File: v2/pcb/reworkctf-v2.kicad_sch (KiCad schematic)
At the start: 35 parts, among them J2 CORTEX_DEBUG_ETM, J6 CONN_01X03, J7 PMOD_HOST, J8 PMOD_HOST, M1 SCREWHOLE, M2 SCREWHOLE, M3 SCREWHOLE, M4 SCREWHOLE, U1 STM32H750XBH6, U3 ECS-1612MV-250-CN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

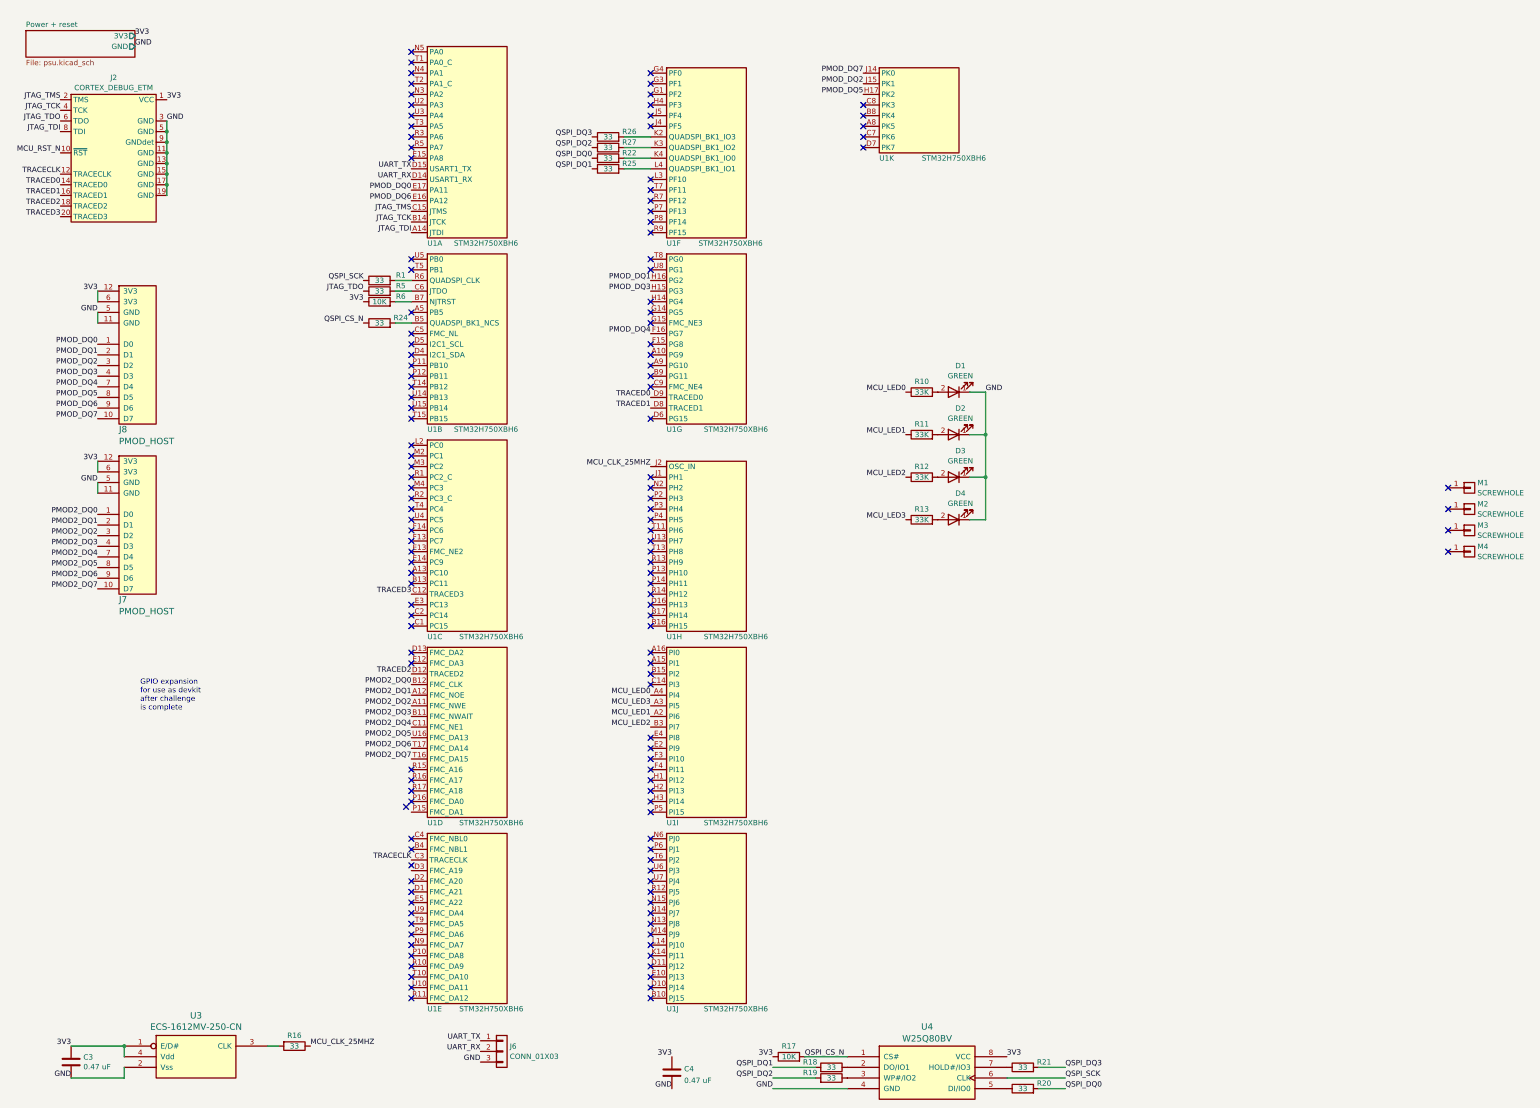
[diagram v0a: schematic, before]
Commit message: Finished initial MCU layout, need to actually add challenges
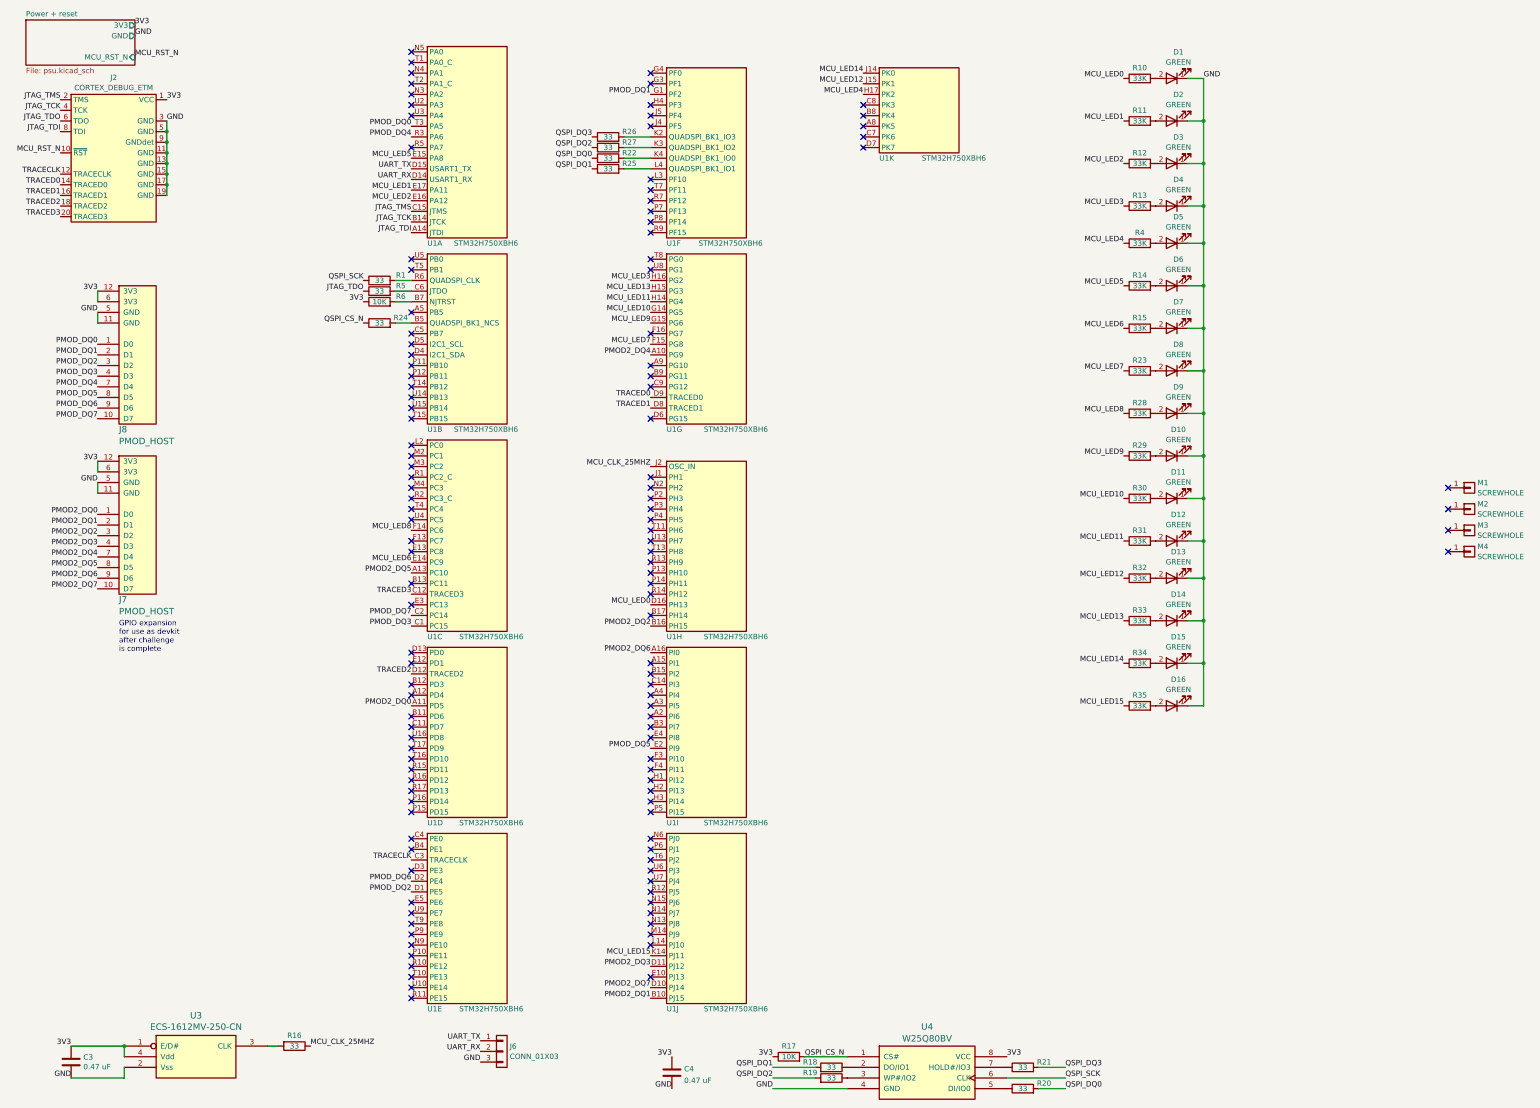
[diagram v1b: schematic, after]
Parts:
- added D10, D11, D12, D13, D14, D15, D16, D5, D6, D7, D8, D9: GREEN, azonenberg_pcb:EIA_0402_LED, symbol device:LED
- added R14, R15, R23, R28, R29, R30, R31, R32, R33, R34, R35, R4: 33K, azonenberg_pcb:EIA_0402_RES_NOSILK, symbol device:R
- M1, M2, M3, M4: footprint (none) -> azonenberg_pcb:MECHANICAL_CLEARANCEHOLE_4_40
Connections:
- net GND: now also D10.1 (K), D11.1 (K), D12.1 (K), D13.1 (K), D14.1 (K), D15.1 (K), D16.1 (K), D5.1 (K), D6.1 (K), D7.1 (K), D8.1 (K), D9.1 (K)
- net MCU_LED0: now also U1.D16 (PH13); no longer U1.A4 (PI4)
- net MCU_LED1: now also U1.E17 (PA11); no longer U1.A2 (PI6)
- net MCU_LED2: now also U1.E16 (PA12); no longer U1.B3 (PI7)
- net MCU_LED3: now also U1.H16 (PG2); no longer U1.A3 (PI5)
- net PMOD2_DQ0: now also U1.A11 (PD5); no longer U1.B12 (PD3)
- net PMOD2_DQ1: now also U1.B10 (PJ15); no longer U1.A12 (PD4)
- net PMOD2_DQ2: now also U1.B16 (PH15); no longer U1.A11 (PD5)
- net PMOD2_DQ3: now also U1.D11 (PJ12); no longer U1.B11 (PD6)
- net PMOD2_DQ4: now also U1.A10 (PG9); no longer U1.C11 (PD7)
- net PMOD2_DQ5: now also U1.A13 (PC10); no longer U1.U16 (PD8)
- net PMOD2_DQ6: now also U1.A16 (PI0); no longer U1.T17 (PD9)
- net PMOD2_DQ7: now also U1.D10 (PJ14); no longer U1.T16 (PD10)
- net PMOD_DQ0: now also U1.T3 (PA5); no longer U1.E17 (PA11)
- net PMOD_DQ1: now also U1.G1 (PF2); no longer U1.H16 (PG2)
- net PMOD_DQ2: now also U1.D1 (PE5); no longer U1.J15 (PK1)
- net PMOD_DQ3: now also U1.C1 (PC15); no longer U1.H15 (PG3)
- net PMOD_DQ4: now also U1.R3 (PA6); no longer U1.F16 (PG7)
- net PMOD_DQ5: now also U1.E2 (PI9); no longer U1.H17 (PK2)
- net PMOD_DQ6: now also U1.D2 (PE4); no longer U1.E16 (PA12)
- net PMOD_DQ7: now also U1.C2 (PC14); no longer U1.J14 (PK0)
- net MCU_LED5: now reaches U1.E15 (PA8)
- net MCU_LED5: now also R14.1
- net MCU_LED7: now reaches U1.F15 (PG8)
- net MCU_LED7: now also R23.1
- net MCU_LED10: now reaches U1.G14 (PG5)
- net MCU_LED10: now also R30.1
- net MCU_LED9: now reaches U1.G15 (PG6)
- net MCU_LED9: now also R29.1
- net MCU_LED11: now reaches U1.H14 (PG4)
- net MCU_LED11: now also R31.1
- net MCU_LED15: now reaches U1.K14 (PJ11)
- net MCU_LED15: now also R35.1
- net MCU_LED6: now reaches U1.E14 (PC9)
- net MCU_LED6: now also R15.1
- net MCU_LED8: now reaches U1.F14 (PC6)
- net MCU_LED8: now also R28.1
- new net: D13.2 (A), R32.2
- new net: D15.2 (A), R34.2
- new net: D9.2 (A), R28.2
- new net: D7.2 (A), R15.2
- new net: D10.2 (A), R29.2
- new net: D6.2 (A), R14.2
- new net: D11.2 (A), R30.2
- new net: D12.2 (A), R31.2
- new net: D14.2 (A), R33.2
- new net: D5.2 (A), R4.2
- new net: D16.2 (A), R35.2
- new net: D8.2 (A), R23.2
- new net MCU_LED12: R32.1, U1.J15 (PK1)
- new net MCU_LED13: R33.1, U1.H15 (PG3)
- new net MCU_LED14: R34.1, U1.J14 (PK0)
- new net MCU_LED4: R4.1, U1.H17 (PK2)
- no-connect marks 137 -> 125
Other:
- sheet Power + reset ports: added MCU_RST_N; removed none
- moved on the sheet: D1, D2, D3, D4, R10, R11, R12, R13

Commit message: Got up to challenge 8
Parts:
- added J3: DOT, azonenberg_pcb:TESTPOINT_SMT_0.5MM, symbol conn:CONN_01X01
- added R36: 10K, azonenberg_pcb:EIA_0201_RES_NOSILK, symbol device:R
- added R37: 10K, azonenberg_pcb:EIA_01005_RES_NOSILK, symbol device:R
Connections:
- net 3V3: now also R36.1, R37.1
- net GND: now also D3.2 (A); no longer D3.1 (K)
- net CHALLENGE_08_A: now reaches U1.T7 (PF11)
- net CHALLENGE_08_A: now also U1.U8 (PG1)
- net CHALLENGE_02_B: now reaches U1.T5 (PB1)
- net CHALLENGE_02_B: now also U1.U4 (PC5)
- net CHALLENGE_02_A: now reaches U1.U5 (PB0)
- net CHALLENGE_02_A: now also U1.U3 (PA4)
- net CHALLENGE_01: now reaches U1.U2 (PA3)
- net CHALLENGE_01: now also J3.1 (P1)
- net at R12.2: now also D3.1 (K); no longer D3.2 (A)
- net CHALLENGE_04: now reaches U1.U6 (PJ3)
- net CHALLENGE_04: now also R36.2
- net CHALLENGE_05: now reaches U1.U7 (PJ4)
- net CHALLENGE_05: now also R37.2
- no-connect marks 125 -> 116
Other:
- moved on the sheet: D3

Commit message: Added challenge 9 with diffpair polarity swap on inner layer
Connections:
- net CHALLENGE_09_N: now reaches U1.P8 (PF14)
- net CHALLENGE_09_N: now also U1.U9 (PE7)
- net CHALLENGE_09_P: now reaches U1.P9 (PE9)
- net CHALLENGE_09_P: now also U1.U10 (PE14)
- no-connect marks 116 -> 112
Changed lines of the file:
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@@
-	)
-	(no_connect
-		(at 109.22 233.68)
 	)
 	(no_connect
@@
 	)
 	(no_connect
-		(at 109.22 246.38)
-	)
-	(no_connect
 		(at 166.37 100.33)
 	)
@@
 	)
 	(no_connect
-		(at 166.37 63.5)
-	)
-	(no_connect
 		(at 109.22 45.72)
 	)
@@
 	)
 	(no_connect
-		(at 109.22 228.6)
-	)
-	(no_connect
 		(at 166.37 110.49)
 	)
@@
 			(width 0)
 			(type default)
+		)
+	)
+	(label "CHALLENGE_09_P"
+		(at 109.22 233.68 180)
+		(effects
+			(font
+				(size 1.27 1.27)
+			)
+			(justify right bottom)
 		)
 	)
@@
 		)
 	)
+	(label "CHALLENGE_09_N"
+		(at 109.22 228.6 180)
+		(effects
+			(font
+				(size 1.27 1.27)
+			)
+			(justify right bottom)
+		)
+	)
 	(label "UART_TX"
 		(at 109.22 50.8 180)
@@
 		)
 	)
+	(label "CHALLENGE_09_P"
+		(at 109.22 246.38 180)
+		(effects
+			(font
+				(size 1.27 1.27)
+			)
+			(justify right bottom)
+		)
+	)
 	(label "MCU_RST_N"
 		(at 43.18 24.13 0)
@@
 		(effects
 			(font
+				(size 1.27 1.27)
+			)
+			(justify right bottom)
+		)
+	)
+	(label "CHALLENGE_09_N"
+		(at 166.37 63.5 180)
+		(effects
+			(font

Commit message: Added challenges 10 and 11 for vias
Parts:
- added R38: 0, azonenberg_pcb:EIA_0402_RES_NOSILK, symbol device:R
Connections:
- net 3V3: now also R38.2
- net CHALLENGE_10: now reaches U1.R9 (PF15)
- net CHALLENGE_10: now also U1.R10 (PE12)
- net CHALLENGE_11: now reaches U1.T13 (PH8)
- net CHALLENGE_11: now also U1.U13 (PH7), R38.1
- no-connect marks 112 -> 108
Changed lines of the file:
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@@
 	)
 	(no_connect
-		(at 109.22 105.41)
-	)
-	(no_connect
 		(at 109.22 238.76)
 	)
@@
 	)
 	(no_connect
-		(at 166.37 142.24)
-	)
-	(no_connect
 		(at 217.17 45.72)
 	)
@@
 	)
 	(no_connect
-		(at 166.37 66.04)
-	)
-	(no_connect
 		(at 109.22 168.91)
 	)
@@
 	)
 	(no_connect
+		(at 109.22 105.41)
+	)
+	(no_connect
 		(at 217.17 43.18)
 	)
@@
 	)
 	(no_connect
-		(at 109.22 241.3)
-	)
-	(no_connect
 		(at 166.37 100.33)
 	)
@@
 	)
 	(no_connect
-		(at 166.37 139.7)
-	)
-	(no_connect
 		(at 109.22 231.14)
 	)
@@
 		)
 	)
+	(label "CHALLENGE_10"
+		(at 166.37 66.04 180)
+		(effects
+			(font
+				(size 1.27 1.27)
+			)
+			(justify right bottom)
+		)
+	)
 	(label "MCU_LED4"
 		(at 217.17 33.02 180)
@@
 		)
 	)
+	(label "CHALLENGE_11"
+		(at 209.55 133.35 180)
+		(effects
+			(font
+				(size 1.27 1.27)
+			)
+			(justify right bottom)
+		)
+	)
 	(label "MCU_LED12"
 		(at 279.4 148.59 180)
@@
 	)
 	(label "3V3"
+		(at 217.17 133.35 0)
+		(effects
+			(font
+				(size 1.27 1.27)
+			)
+			(justify left bottom)
+		)
+	)
+	(label "3V3"
 		(at 195.58 262.89 180)
 		(effects
@@
 		)
 	)
+	(label "CHALLENGE_11"
+		(at 166.37 139.7 180)
+		(effects
+			(font
+				(size 1.27 1.27)
+			)
+			(justify right bottom)
+		)
+	)
 	(label "CHALLENGE_04"
 		(at 166.37 218.44 180)
@@
 		)
 	)
+	(label "CHALLENGE_11"
+		(at 166.37 142.24 180)
+		(effects
+			(font
+				(size 1.27 1.27)
+			)
+			(justify right bottom)
+		)
+	)
 	(label "MCU_LED5"
 		(at 109.22 48.26 180)
@@
 		)
 	)
+	(label "CHALLENGE_10"
+		(at 109.22 241.3 180)
+		(effects
+			(font
+				(size 1.27 1.27)
+			)
+			(justify right bottom)
+		)
+	)
 	(label "MCU_LED3"
 		(at 166.37 77.47 180)
@@
 				)
 			)
+		)
+	)
+	(symbol
+		(lib_id "device:R")
+		(at 213.36 133.35 90)
+		(unit 1)
+		(exclude_from_sim no)
+		(in_bom yes)
+		(on_board yes)
+		(dnp no)
+		(fields_autoplaced yes)
+		(property "Reference" "R38"
+			(at 213.36 128.1895 90)
+			(effects
+				(font
+					(size 1.27 1.27)
+				)
+			)
+		)
+		(property "Value" "0"
+			(at 213.36 130.6138 90)
+			(effects
+				(font
+					(size 1.27 1.27)
+				)
+			)
+		)
+		(property "Footprint" "azonenberg_pcb:EIA_0402_RES_NOSILK"
+			(at 213.36 135.128 90)
+			(effects
+				(font
+					(size 1.27 1.27)
+				)
+				(hide yes)
+			)
+		)
+		(property "Datasheet" ""
+			(at 213.36 133.35 0)
+			(effects
+				(font
+					(size 1.27 1.27)
+				)
+				(hide yes)
+			)
+		)
+		(property "Description" "Resistor"
+			(at 213.36 133.35 0)
+			(effects
+				(font
+					(size 1.27 1.27)
+				)
+				(hide yes)
+			)
+		)
+		(pin "2"
+		)
+		(pin "1"
+		)
+		(instances
+			(project "reworkctf-v2"
+				(path "/2cafc55c-39dd-4b2d-b0b4-dd03e5652b07"
+					(reference "R38")
+					(unit 1)
+				)
+			)

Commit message: Added SM-2 challenge, shrunk overall PCB footprint a bunch
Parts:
- added M5: OSHW, w_logo:Logo_silk_OSHW_6x6mm, symbol special-azonenberg:MECHANICAL
- added M6: LONGTHING, azonenberg_pcb:LONGTHING-1200DPI, symbol special-azonenberg:MECHANICAL
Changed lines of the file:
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@@
 	)
 	(symbol
+		(lib_id "special-azonenberg:MECHANICAL")
+		(at 360.68 156.21 0)
+		(unit 1)
+		(exclude_from_sim no)
+		(in_bom yes)
+		(on_board yes)
+		(dnp no)
+		(fields_autoplaced yes)
+		(property "Reference" "M6"
+			(at 363.855 154.9978 0)
+			(effects
+				(font
+					(size 1.27 1.27)
+				)
+				(justify left)
+			)
+		)
+		(property "Value" "LONGTHING"
+			(at 363.855 157.4221 0)
+			(effects
+				(font
+					(size 1.27 1.27)
+				)
+				(justify left)
+			)
+		)
+		(property "Footprint" "azonenberg_pcb:LONGTHING-1200DPI"
+			(at 360.68 156.21 0)
+			(effects
+				(font
+					(size 1.27 1.27)
+				)
+				(hide yes)
+			)
+		)
+		(property "Datasheet" ""
+			(at 360.68 156.21 0)
+			(effects
+				(font
+					(size 1.27 1.27)
+				)
+				(hide yes)
+			)
+		)
+		(property "Description" ""
+			(at 360.68 156.21 0)
+			(effects
+				(font
+					(size 1.27 1.27)
+				)
+				(hide yes)
+			)
+		)
+		(instances
+			(project "reworkctf-v2"
+				(path "/2cafc55c-39dd-4b2d-b0b4-dd03e5652b07"
+					(reference "M6")
+					(unit 1)
+				)
+			)
+		)
+	)
+	(symbol
 		(lib_id "device:R")
 		(at 283.21 119.38 90)
@@
 					(unit 1)
 				)
+			)
+		)
+	)
+	(symbol
+		(lib_id "special-azonenberg:MECHANICAL")
+		(at 360.68 149.86 0)
+		(unit 1)
+		(exclude_from_sim no)
+		(in_bom yes)
+		(on_board yes)
+		(dnp no)
+		(fields_autoplaced yes)
+		(property "Reference" "M5"
+			(at 363.855 148.6478 0)
+			(effects
+				(font
+					(size 1.27 1.27)
+				)
+				(justify left)
+			)
+		)
+		(property "Value" "OSHW"
+			(at 363.855 151.0721 0)
+			(effects
+				(font
+					(size 1.27 1.27)
+				)
+				(justify left)
+			)
+		)
+		(property "Footprint" "w_logo:Logo_silk_OSHW_6x6mm"
+			(at 360.68 149.86 0)
+			(effects
+				(font
+					(size 1.27 1.27)
+				)
+				(hide yes)
+			)
+		)
+		(property "Datasheet" ""
+			(at 360.68 149.86 0)
+			(effects
+				(font
+					(size 1.27 1.27)
+				)
+				(hide yes)
+			)
+		)
+		(property "Description" ""
+			(at 360.68 149.86 0)
+			(effects
+				(font
+					(size 1.27 1.27)
+				)
+				(hide yes)
+			)
+		)
+		(instances
+			(project "reworkctf-v2"
+				(path "/2cafc55c-39dd-4b2d-b0b4-dd03e5652b07"
+					(reference "M5")
+					(unit 1)
+				)

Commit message: Added challenge 15 (missing pullup)
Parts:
- added J4: TESTPOINT, azonenberg_pcb:TESTPOINT_SMT_0.5MM, symbol conn:CONN_01X01
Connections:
- net CHALLENGE_14: now reaches U1.P11 (PB10)
- net CHALLENGE_14: now also U1.R13 (PH9)
- net CHALLENGE_13: now reaches U1.T14 (PB12)
- net CHALLENGE_13: now also U1.U14 (PB13)
- net CHALLENGE_12: now reaches U1.A2 (PI6)
- net CHALLENGE_12: now also U1.A3 (PI5), J4.1 (P1)
- net CHALLENGE_15: now reaches U1.E3 (PC13)
- no-connect marks 108 -> 101
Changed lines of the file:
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@@
 	)
 	(no_connect
+		(at 109.22 100.33)
+	)
+	(no_connect
 		(at 109.22 127)
 	)
@@
 	)
 	(no_connect
-		(at 109.22 154.94)
-	)
-	(no_connect
 		(at 166.37 152.4)
 	)
@@
 	)
 	(no_connect
-		(at 109.22 100.33)
-	)
-	(no_connect
 		(at 166.37 194.31)
 	)
@@
 	)
 	(no_connect
-		(at 109.22 105.41)
-	)
-	(no_connect
 		(at 217.17 43.18)
 	)
@@
 	)
 	(no_connect
-		(at 166.37 179.07)
-	)
-	(no_connect
 		(at 166.37 35.56)
 	)
@@
 	)
 	(no_connect
-		(at 166.37 181.61)
-	)
-	(no_connect
-		(at 109.22 97.79)
-	)
-	(no_connect
 		(at 109.22 95.25)
 	)
@@
 	)
 	(no_connect
-		(at 109.22 102.87)
-	)
-	(no_connect
 		(at 166.37 228.6)
 	)
@@
 	)
 	(no_connect
-		(at 166.37 144.78)
-	)
-	(no_connect
 		(at 166.37 231.14)
 	)
@@
 	(wire
 		(pts
+			(xy 147.32 179.07) (xy 166.37 179.07)
+		)
+		(stroke
+			(width 0)
+			(type default)
+		)
+	)
+	(wire
+		(pts
 			(xy 294.64 39.37) (xy 298.45 39.37)
 		)
@@
 		)
 	)
+	(label "CHALLENGE_14"
+		(at 109.22 97.79 180)
+		(effects
+			(font
+				(size 1.27 1.27)
+			)
+			(justify right bottom)
+		)
+	)
 	(label "PMOD_DQ3"
 		(at 109.22 160.02 180)
@@
 		)
 	)
+	(label "CHALLENGE_14"
+		(at 166.37 144.78 180)
+		(effects
+			(font
+				(size 1.27 1.27)
+			)
+			(justify right bottom)
+		)
+	)
 	(label "CHALLENGE_10"
 		(at 166.37 66.04 180)
@@
 		)
 	)
+	(label "CHALLENGE_13"
+		(at 109.22 105.41 180)
+		(effects
+			(font
+				(size 1.27 1.27)
+			)
+			(justify right bottom)
+		)
+	)
 	(label "PMOD2_DQ0"
 		(at 109.22 179.07 180)
@@
 		)
 	)
+	(label "CHALLENGE_13"
+		(at 109.22 102.87 180)
+		(effects
+			(font
+				(size 1.27 1.27)
+			)
+			(justify right bottom)
+		)
+	)
 	(label "MCU_LED9"
 		(at 279.4 119.38 180)
@@
 		)
 	)
+	(label "CHALLENGE_15"
+		(at 109.22 154.94 180)
+		(effects
+			(font
+				(size 1.27 1.27)
+			)
+			(justify right bottom)
+		)
+	)
 	(label "3V3"
 		(at 195.58 262.89 180)
@@
 		)
 	)
+	(label "CHALLENGE_12"
+		(at 166.37 181.61 180)
+		(effects
+			(font
+				(size 1.27 1.27)
+			)
+			(justify right bottom)
+		)
+	)
 	(label "MCU_RST_N"
 		(at 43.18 24.13 0)
@@
 		)
 	)
+	(label "CHALLENGE_12"
+		(at 166.37 179.07 180)
+		(effects
+			(font
+				(size 1.27 1.27)
+			)
+			(justify right bottom)
+		)
+	)
 	(label "TRACED1"
 		(at 166.37 107.95 180)
@@
 				)
 			)
+		)
+	)
+	(symbol
+		(lib_id "conn:CONN_01X01")
+		(at 142.24 179.07 180)
+		(unit 1)
+		(exclude_from_sim no)
+		(in_bom yes)
+		(on_board yes)
+		(dnp no)
+		(fields_autoplaced yes)
+		(property "Reference" "J4"
+			(at 142.24 173.7825 0)
+			(effects
+				(font
+					(size 1.27 1.27)
+				)
+			)
+		)
+		(property "Value" "TESTPOINT"
+			(at 142.24 176.2068 0)
+			(effects
+				(font
+					(size 1.27 1.27)
+				)
+			)
+		)
+		(property "Footprint" "azonenberg_pcb:TESTPOINT_SMT_0.5MM"
+			(at 142.24 179.07 0)
+			(effects
+				(font
+					(size 1.27 1.27)
+				)
+				(hide yes)
+			)
+		)
+		(property "Datasheet" ""
+			(at 142.24 179.07 0)
+			(effects
+				(font
+					(size 1.27 1.27)
+				)
+				(hide yes)
+			)
+		)
+		(property "Description" "Connector, single row, 01x01, pin header"
+			(at 142.24 179.07 0)
+			(effects
+				(font
+					(size 1.27 1.27)
+				)
+				(hide yes)
+			)
+		)
+		(pin "1"
+		)
+		(instances
+			(project "reworkctf-v2"
+				(path "/2cafc55c-39dd-4b2d-b0b4-dd03e5652b07"
+					(reference "J4")
+					(unit 1)
+				)
+			)

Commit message: Initial work on "free play area" sandbox
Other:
- added sheet Free Play Area (free-play.kicad_sch)
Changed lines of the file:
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@@
+		)
+	)
+	(sheet
+		(at 344.805 16.51)
+		(size 31.115 24.765)
+		(exclude_from_sim no)
+		(in_bom yes)
+		(on_board yes)
+		(dnp no)
+		(fields_autoplaced yes)
+		(stroke
+			(width 0.1524)
+			(type solid)
+		)
+		(fill
+			(color 0 0 0 0.0000)
+		)
+		(property "Sheetname" "Free Play Area"
+			(at 344.805 15.7984 0)
+			(effects
+				(font
+					(size 1.27 1.27)
+				)
+				(justify left bottom)
+			)
+		)
+		(property "Sheetfile" "free-play.kicad_sch"
+			(at 344.805 41.8596 0)
+			(effects
+				(font
+					(size 1.27 1.27)
+				)
+				(justify left top)
+			)
+		)
+		(instances
+			(project "reworkctf-v2"
+				(path "/2cafc55c-39dd-4b2d-b0b4-dd03e5652b07"
+					(page "3")
+				)
+			)
 		)
 	)
